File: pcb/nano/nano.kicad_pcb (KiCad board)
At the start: 2 copper layers, 8 parts

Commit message: Added pin numbers to Serial pins. M3 hole text now fully inside the edge cuts.
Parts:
- gave numbers to parts that had none: 1
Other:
- board text added: "MISO (D12)"
- board text added: "MOSI (D11)"
- board text added: "RXD (D0)"
- board text added: "SCK (D13)"
- board text added: "SCL (A5)"
- board text added: "SDA (A4)"
- board text added: "TXD (D1)"
- board text removed: "MISO"
- board text removed: "MOSI"
- board text removed: "RXD"
- board text removed: "SCK"
- board text removed: "SCL"
- board text removed: "SDA"
- board text removed: "TXD"
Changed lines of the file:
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@@
   )
   (setup
-    (last_trace_width 0.5)
+    (last_trace_width 0.25)
     (user_trace_width 0.5)
     (user_trace_width 0.5)
@@
     (descr "Mounting Hole 3.2mm, no annular, M3")
     (tags "mounting hole 3.2mm no annular m3")
-    (fp_text reference "" (at 0 -4.2) (layer F.Fab)
+    (fp_text reference X (at 0 0) (layer F.Fab)
       (effects (font (size 1 1) (thickness 0.15)))
     )
@@
     (descr "Mounting Hole 3.2mm, no annular, M3")
     (tags "mounting hole 3.2mm no annular m3")
-    (fp_text reference "" (at 0 -4.2) (layer F.Fab)
+    (fp_text reference X (at 0 0) (layer F.Fab)
       (effects (font (size 1 1) (thickness 0.15)))
     )
@@
     (effects (font (size 1.5 1.5) (thickness 0.3)))
   )
-  (gr_text MISO (at 132.08 37.465 270) (layer F.SilkS)
+  (gr_text "MISO (D12)" (at 132.08 37.465 270) (layer F.SilkS)
     (effects (font (size 1 1) (thickness 0.2)) (justify left))
   )
@@
     (effects (font (size 1.5 1.5) (thickness 0.3)) (justify left mirror))
   )
-  (gr_text SCK (at 129.54 37.465 270) (layer F.SilkS)
-    (effects (font (size 1 1) (thickness 0.2)) (justify left))
-  )
-  (gr_text RXD (at 147.32 37.465 270) (layer F.SilkS)
-    (effects (font (size 1 1) (thickness 0.2)) (justify left))
-  )
-  (gr_text SCL (at 142.24 37.465 270) (layer F.SilkS)
-    (effects (font (size 1 1) (thickness 0.2)) (justify left))
-  )
-  (gr_text SDA (at 139.7 37.465 270) (layer F.SilkS)
-    (effects (font (size 1 1) (thickness 0.2)) (justify left))
-  )
-  (gr_text TXD (at 144.78 37.465 270) (layer F.SilkS)
+  (gr_text "SCK (D13)" (at 129.54 37.465 270) (layer F.SilkS)
+    (effects (font (size 1 1) (thickness 0.2)) (justify left))
+  )
+  (gr_text "RXD (D0)" (at 147.32 37.465 270) (layer F.SilkS)
+    (effects (font (size 1 1) (thickness 0.2)) (justify left))
+  )
+  (gr_text "SCL (A5)" (at 142.24 37.465 270) (layer F.SilkS)
+    (effects (font (size 1 1) (thickness 0.2)) (justify left))
+  )
+  (gr_text "SDA (A4)" (at 139.7 37.465 270) (layer F.SilkS)
+    (effects (font (size 1 1) (thickness 0.2)) (justify left))
+  )
+  (gr_text "TXD (D1)" (at 144.78 37.465 270) (layer F.SilkS)
     (effects (font (size 1 1) (thickness 0.2)) (justify left))
   )
@@
     (effects (font (size 1 1) (thickness 0.2)) (justify left))
   )
-  (gr_text MOSI (at 134.62 37.465 270) (layer F.SilkS)
-    (effects (font (size 1 1) (thickness 0.2)) (justify left))
-  )
+  (gr_text "MOSI (D11)" (at 134.62 37.465 270) (layer F.SilkS)
+    (effects (font (size 1 1) (thickness 0.2)) (justify left))
+  )

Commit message: Added a Rotary Encoder module. Tidied up a couple of modules before printing them.
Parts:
- added J2: Header2, Pin_Headers:Pin_Header_Straight_1x15_Pitch2.54mm, F.Cu at (146.1, 69.8)
- added J3: Header1, Pin_Headers:Pin_Header_Straight_1x15_Pitch2.54mm, F.Cu at (146.1, 47.0)
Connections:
- O3 pad 10: /A5 -> /A2
- O3 pad 11: /A6 -> /A1
- O3 pad 12: /A7 -> /A0
- O3 pad 5: /A0 -> /A7
- O3 pad 6: /A1 -> /A6
- O3 pad 7: /A2 -> /A5
- O3 pad 8: /A3 -> /A4
- O3 pad 9: /A4 -> /A3
- XA1 pad 3V3: (no net) -> /3V3
- XA1 pad AREF: (no net) -> /AREF
- XA1 pad RST1: (no net) -> /Reset1
- XA1 pad RST2: (no net) -> /Reset2
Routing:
- net /GND: track 0.00 -> 31.4 mm, vias 0 -> 3
- net /A0: track 27.9 -> 15.8 mm
- net /A7: track 27.2 -> 15.1 mm, vias 1 -> 0
- net /A1: track 25.7 -> 15.1 mm, vias 2 -> 0
- net /A6: track 22.9 -> 15.8 mm, vias 2 -> 0
- net /A2: track 21.0 -> 15.1 mm, vias 2 -> 0
- net /D9: track 44.7 -> 48.5 mm
- net /D7: track 37.5 -> 41.3 mm
- net /D4: track 26.8 -> 30.6 mm
- net /Reset1: track 0.00 -> 3.81 mm
- net /D8: track 41.1 -> 44.9 mm
- net /D6: track 33.9 -> 37.8 mm
- net /D5: track 30.4 -> 34.2 mm
- net /D3: track 23.2 -> 27.0 mm
- net /D2: track 20.6 -> 24.4 mm
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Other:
- board text added: "Arduino Nano v1.0 nickthecoder.co.uk"
- board text removed: "Arduino Nano"
- board text removed: "Arduino Nano V1.0 nickthecoder.co.uk"

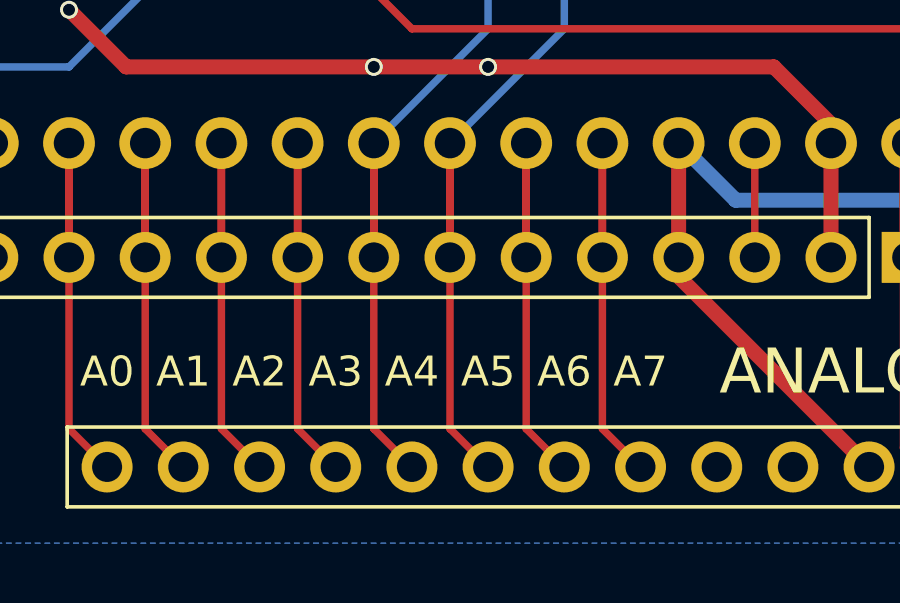
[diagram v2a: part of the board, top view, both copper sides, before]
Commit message: Added README.md for each of the modules, plus a few minor tweaks to PCB layouts while writing the text.
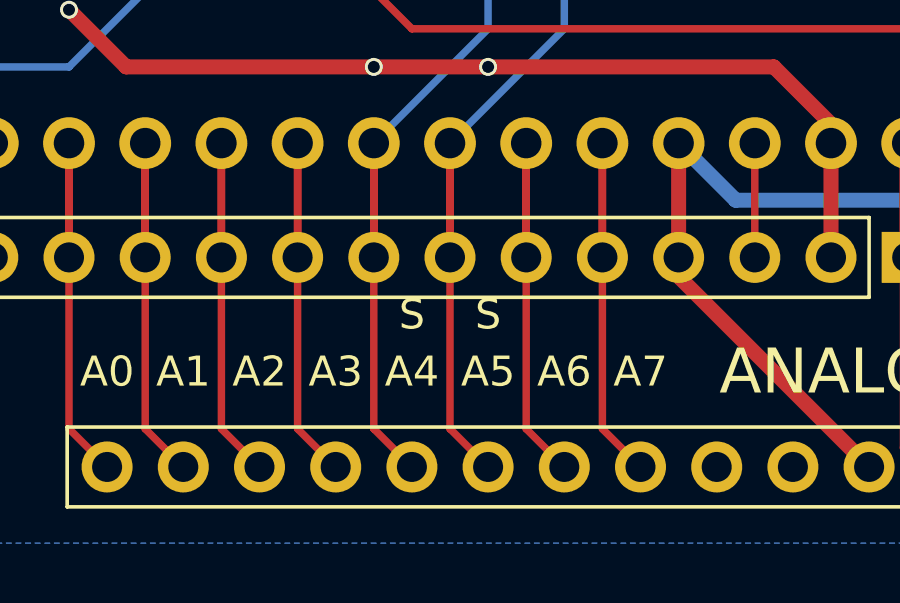
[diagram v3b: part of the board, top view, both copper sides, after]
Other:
- board text added: "S"
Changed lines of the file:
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@@
     (area 104.626999 31.115 158.115001 80.645001)
     (thickness 1.6)
-    (drawings 29)
+    (drawings 31)
     (tracks 159)
     (zones 0)
@@
   )
   (setup
-    (last_trace_width 0.5)
+    (last_trace_width 0.25)
     (user_trace_width 0.5)
     (user_trace_width 0.5)
@@
     )
   )
+  (gr_text S (at 129.54 71.755) (layer F.SilkS)
+    (effects (font (size 1 1) (thickness 0.2)))
+  )
+  (gr_text S (at 132.08 71.755) (layer F.SilkS)
+    (effects (font (size 1 1) (thickness 0.2)))
+  )
   (gr_text "Arduino Nano v1.0\nnickthecoder.co.uk" (at 129.54 58.42) (layer F.SilkS)
